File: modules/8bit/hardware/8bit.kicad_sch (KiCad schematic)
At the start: 48 parts, among them J1 PJ301M-12, J2 PJ301M-12, J3 PJ301M-12, J4 Eurorack_2x5, J5 UPDI, Q1 MMBT3904, SW1 MODE, U1 ATtiny1616-MNR, U2 HT7550-1, U3 TL072, U4 MCP6001

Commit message: Set proper output resistors to match with the voltage.
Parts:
- R12: LCSC C4410 -> C2074262; MPN 1206W4F1001T5E -> ESR18EZPF1001; Manufacturer UNI-ROYAL -> ROHM Semicon; Note Output series: short / mis-patch current limit (op-amp also current-limits) -> Output series: short / mis-patch current limit (op-amp also current-limits); 0.5 W for a permanent +/-12 V mis-patch (0.28 W); Power 0.25W -> 0.5W
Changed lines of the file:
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@@
 			)
 		)
-		(property "Power" "0.25W"
+		(property "Power" "0.5W"
 			(at 304.8 160.02 90)
 			(hide yes)
@@
 			)
 		)
-		(property "Note" "Output series: short / mis-patch current limit (op-amp also current-limits)"
+		(property "Note" "Output series: short / mis-patch current limit (op-amp also current-limits); 0.5 W for a permanent +/-12 V mis-patch (0.28 W)"
 			(at 304.8 160.02 90)
 			(hide yes)
@@
 			)
 		)
-		(property "LCSC" "C4410"
+		(property "LCSC" "C2074262"
 			(at 304.8 160.02 90)
 			(hide yes)
@@
 			)
 		)
-		(property "MPN" "1206W4F1001T5E"
+		(property "MPN" "ESR18EZPF1001"
 			(at 304.8 160.02 90)
 			(hide yes)
@@
 			)
 		)
-		(property "Manufacturer" "UNI-ROYAL"
+		(property "Manufacturer" "ROHM Semicon"
 			(at 304.8 160.02 90)
 			(hide yes)

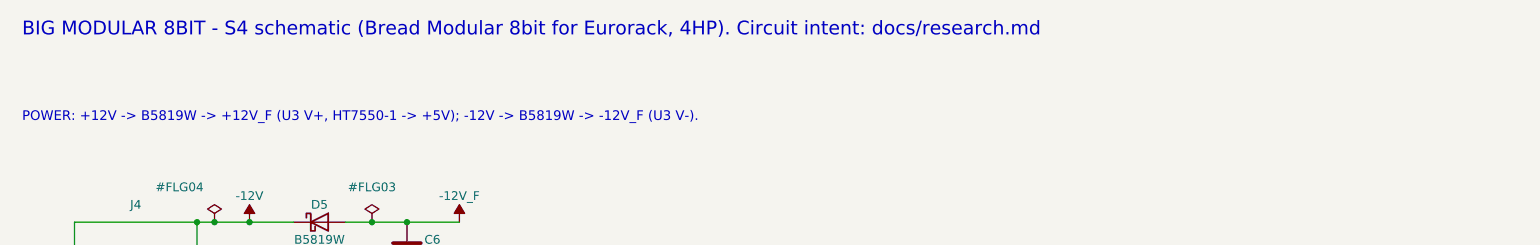
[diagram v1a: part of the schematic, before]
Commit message: Update the 8bit switch to a DIP version.
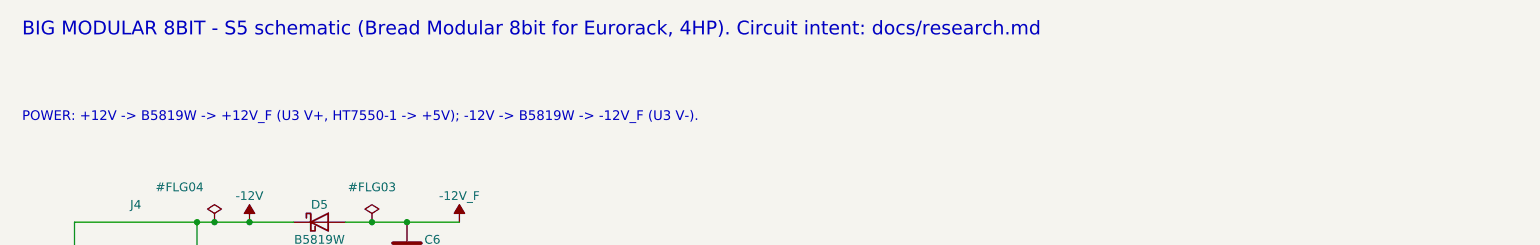
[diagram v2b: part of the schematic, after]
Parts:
- SW1: footprint 8BIT:K2-1808SN-A4SW-01 -> 8BIT:SW_PUSH_6mm_H7.3mm; MPN K2-1808SN-A4SW-01 -> 6x6x7 mm THT tact switch, 4 pins (generic); Manufacturer Korean Hroparts Elec -> (none); Note Mode button = Bread Modular SW1 (LCSC C92589, 4.2 x 3.25 x 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 -> Mode button (as Bread Modular SW1, PA4 internal pull-up): g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
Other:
- note added: "BIG MODULAR 8BIT - S5 schematic (Bread Modular 8bit for Eurorack, 4HP). Circuit intent: docs/research.md"
- note removed: "BIG MODULAR 8BIT - S4 schematic (Bread Modular 8bit for Eurorack, 4HP). Circuit intent: docs/research.md"
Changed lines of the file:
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@@
 	(title_block
 		(title "Big Modular - 8bit")
-		(rev "S4")
+		(rev "S5")
 		(company "Big Modular")
-		(comment 1 "SCHEMATIC S4 - Bread Modular 8bit for Eurorack: protected MIDI in, bipolar buffered CV in, knob 3 passive LPF, +/-5 V out")
+		(comment 1 "SCHEMATIC S5 - Bread Modular 8bit for Eurorack: protected MIDI in, bipolar buffered CV in, knob 3 passive LPF, +/-5 V out")
 		(comment 2 "Circuit intent: docs/research.md; placement: docs/geometry.json")
 	)
-	(text "BIG MODULAR 8BIT - S4 schematic (Bread Modular 8bit for Eurorack, 4HP). Circuit intent: docs/research.md"
+	(text "BIG MODULAR 8BIT - S5 schematic (Bread Modular 8bit for Eurorack, 4HP). Circuit intent: docs/research.md"
 		(exclude_from_sim no)
 		(at 20.32 17.78 0)
@@
 			)
 		)
-		(property "Footprint" "8BIT:K2-1808SN-A4SW-01"
+		(property "Footprint" "8BIT:SW_PUSH_6mm_H7.3mm"
 			(at 213.36 111.76 90)
 			(hide yes)
@@
 			)
 		)
-		(property "MPN" "K2-1808SN-A4SW-01"
+		(property "MPN" "6x6x7 mm THT tact switch, 4 pins (generic)"
 			(at 213.36 111.76 90)
 			(hide yes)
@@
 			)
 		)
-		(property "Manufacturer" "Korean Hroparts Elec"
-			(at 213.36 111.76 90)
-			(hide yes)
-			(show_name no)
-			(do_not_autoplace no)
-			(effects
-				(font
-					(size 1.27 1.27)
-				)
-			)
-		)
-		(property "Note" "Mode button = Bread Modular SW1 (LCSC C92589, 4.2 x 3.25 x 2.5 mm SMD tact), PA4 internal pull-up. Hand-soldered on the F side; pressed through the panel by the printed actuator (panels/button-actuator)"
+		(property "Note" "Mode button (as Bread Modular SW1, PA4 internal pull-up): generic 6 x 6 mm THT tact, 7 mm tall, Ø3.5 round stem, pins 6.5 x 4.5 mm. Hand-soldered on the F side; pressed through the panel by the printed cap (panels/button-actuator)"
 			(at 213.36 111.76 90)
 			(hide yes)
